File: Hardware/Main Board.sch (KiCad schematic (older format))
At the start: 0 parts

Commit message: Merge Danny's changes to the board, gitignore
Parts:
- added .1uF: C5, symbol CAPACITOR
- added .1uF: C6, symbol CAPACITOR
- added .1uF: C7, symbol CAPACITOR
- added .1uF: C3, symbol CAPACITOR
- added .1uF: C2, symbol CAPACITOR
- added .1uF: C1, symbol CAPACITOR
- added .1uF: C8, symbol CAPACITOR
- added .1uF: C9, symbol CAPACITOR
- added 4.7uF: C4, symbol CAPACITOR
- added C1: 4.7uF, symbol CAPACITOR
- added C2: .1uF, symbol CAPACITOR
- added C3, C4: 15pF, symbol CAPACITOR
- added FB?: FB1, symbol FERRITE
- added U1: STM32F401RCT6, symbol STM32F401RCT6
- added X1: 24MHz, ~, symbol CRYSTAL
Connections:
- net labels added: GND, NRST, OSC_IN, OSC_OUT, Reg+3v3, VDD, VDDA
- wire segments 0 -> 64

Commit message: Add 5v regulator and RS485 transceiver to Main board
Added RS485 and a 5v regulator to power it
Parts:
- added U1: SN75176BDR, symbol SN75176BDR
- .1uF, 4.7uF, C1, C2, C3, C4: symbol CAPACITOR -> Capacitor
- FB?: symbol FERRITE -> Ferrite
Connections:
- net labels added: 485_A, 485_B, GPIO_PC4_Reg1EN, GPIO_PC5_Reg2EN, Reg+3V3, Reg+5V, USART1_RX, USART1_TX
- wire segments 64 -> 83

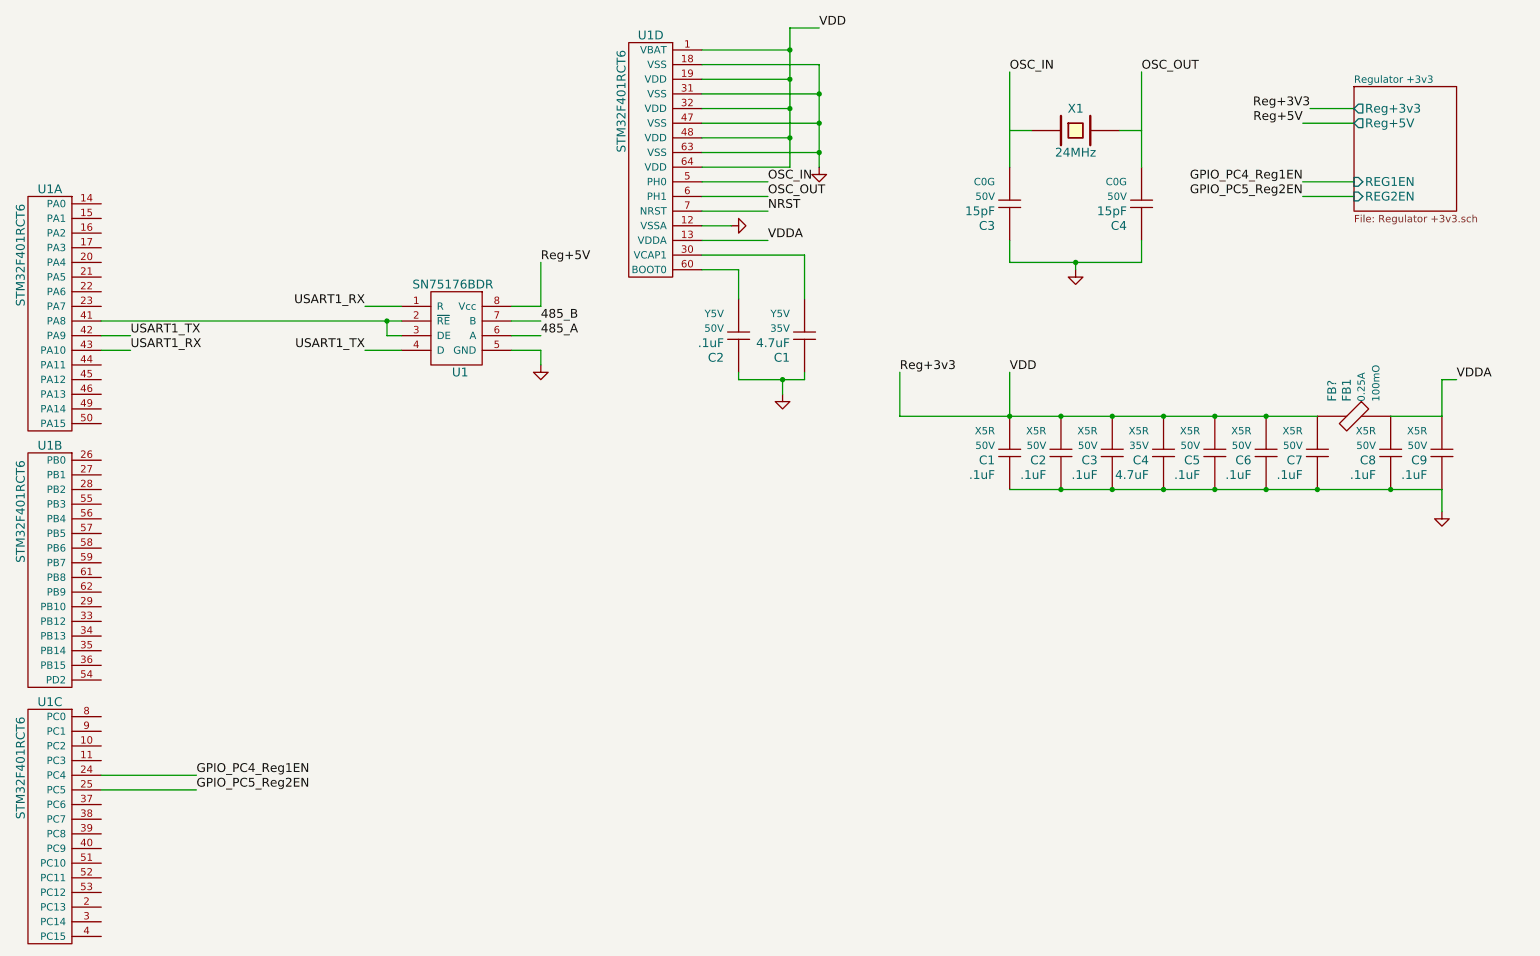
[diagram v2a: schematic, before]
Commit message: Add BTA breakout for Vernier sensors and convert 5v analog to 3v3
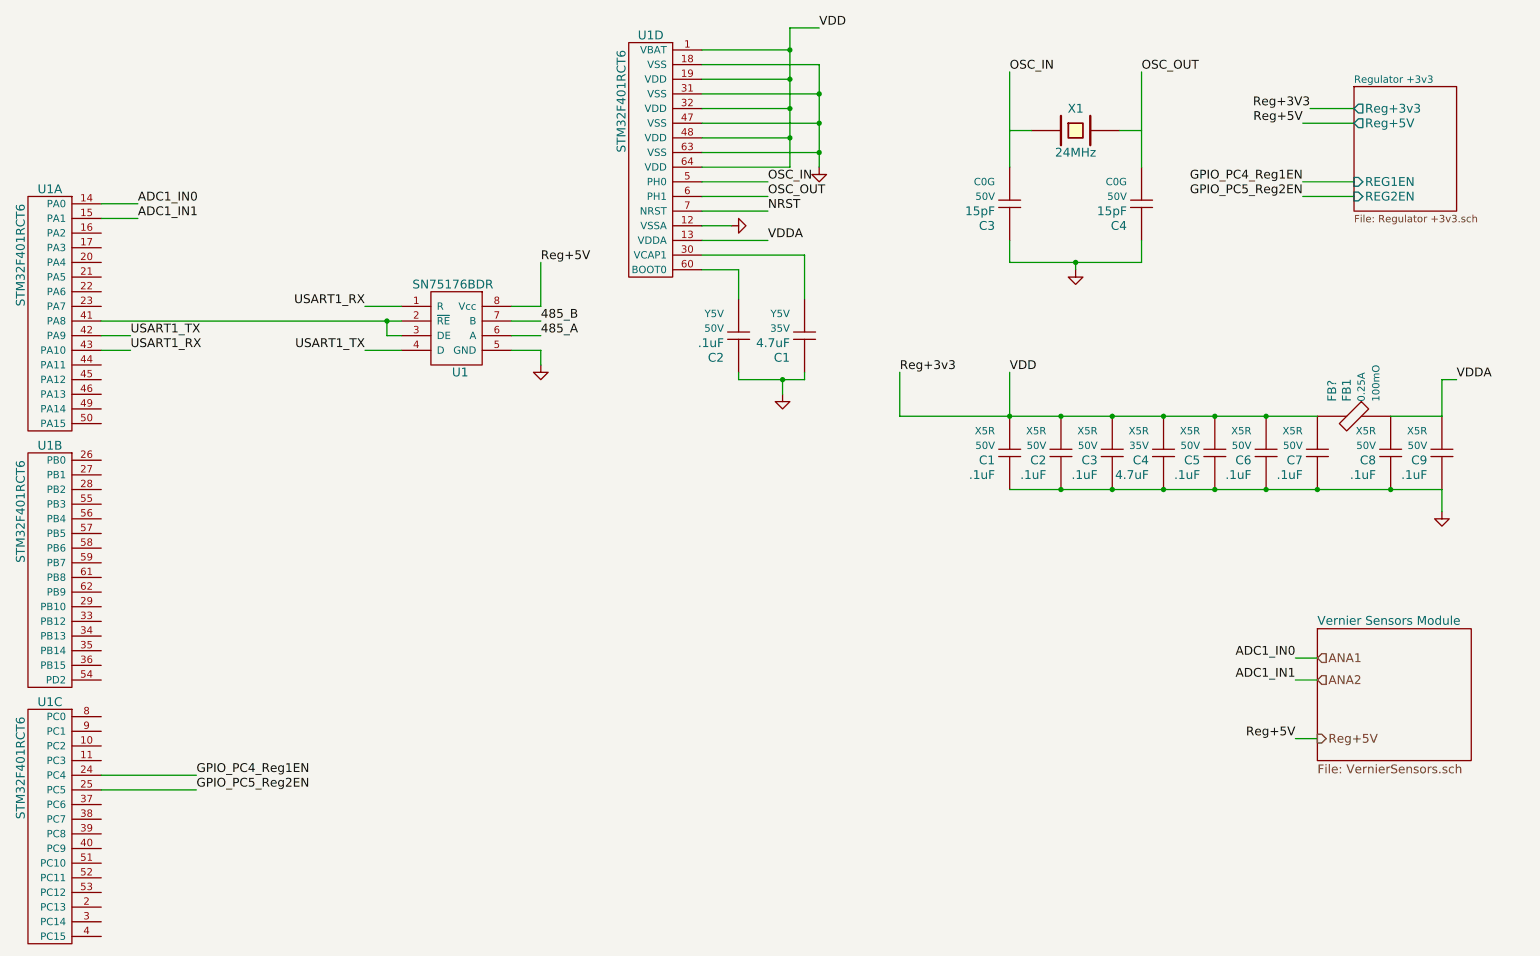
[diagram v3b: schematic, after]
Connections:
- net ANA1: now reaches U1.14 (PA0)
- net ANA2: now reaches U1.15 (PA1)
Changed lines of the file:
@@
 LIBS:device
 LIBS:conn
+LIBS:MAVRIClib
 LIBS:Passives
 LIBS:STMicroelectronics
-LIBS:MAVRIClib
 LIBS:Main Board-cache
 EELAYER 25 0
@@
 $Descr A4 11693 8268
 encoding utf-8
-Sheet 1 2
+Sheet 1 3
 Title ""
 Date "7 mar 2015"
@@
 Text Label 4200 2700 0    60   ~ 0
 485_A
+Text HLabel 9500 5450 2    60   Output ~ 0
+Reg+5V
+Text Label 9350 5450 2    60   ~ 0
+Reg+5V
+$Sheet
+S 9500 4700 1050 900
+U 551DB2D0
+F0 "Vernier Sensors Module" 60
+F1 "VernierSensors.sch" 60
+$EndSheet
+Wire Wire Line
+	9500 5450 9350 5450
+Text HLabel 9500 4900 2    60   Input ~ 0
+ANA1
+Text HLabel 9500 5050 2    60   Input ~ 0
+ANA2
+Wire Wire Line
+	9500 4900 9350 4900
+Wire Wire Line
+	9500 5050 9350 5050
+Text Label 9350 4900 2    60   ~ 0
+ADC1_IN0
+Text Label 9350 5050 2    60   ~ 0
+ADC1_IN1
+Wire Wire Line
+	1200 1800 1450 1800
+Wire Wire Line
+	1450 1900 1200 1900
+Text Label 1450 1900 0    60   ~ 0
+ADC1_IN1
+Text Label 1450 1800 0    60   ~ 0
+ADC1_IN0
 $EndSCHEMATC

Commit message: Add 485 network out, POE for Wheel Pod boards
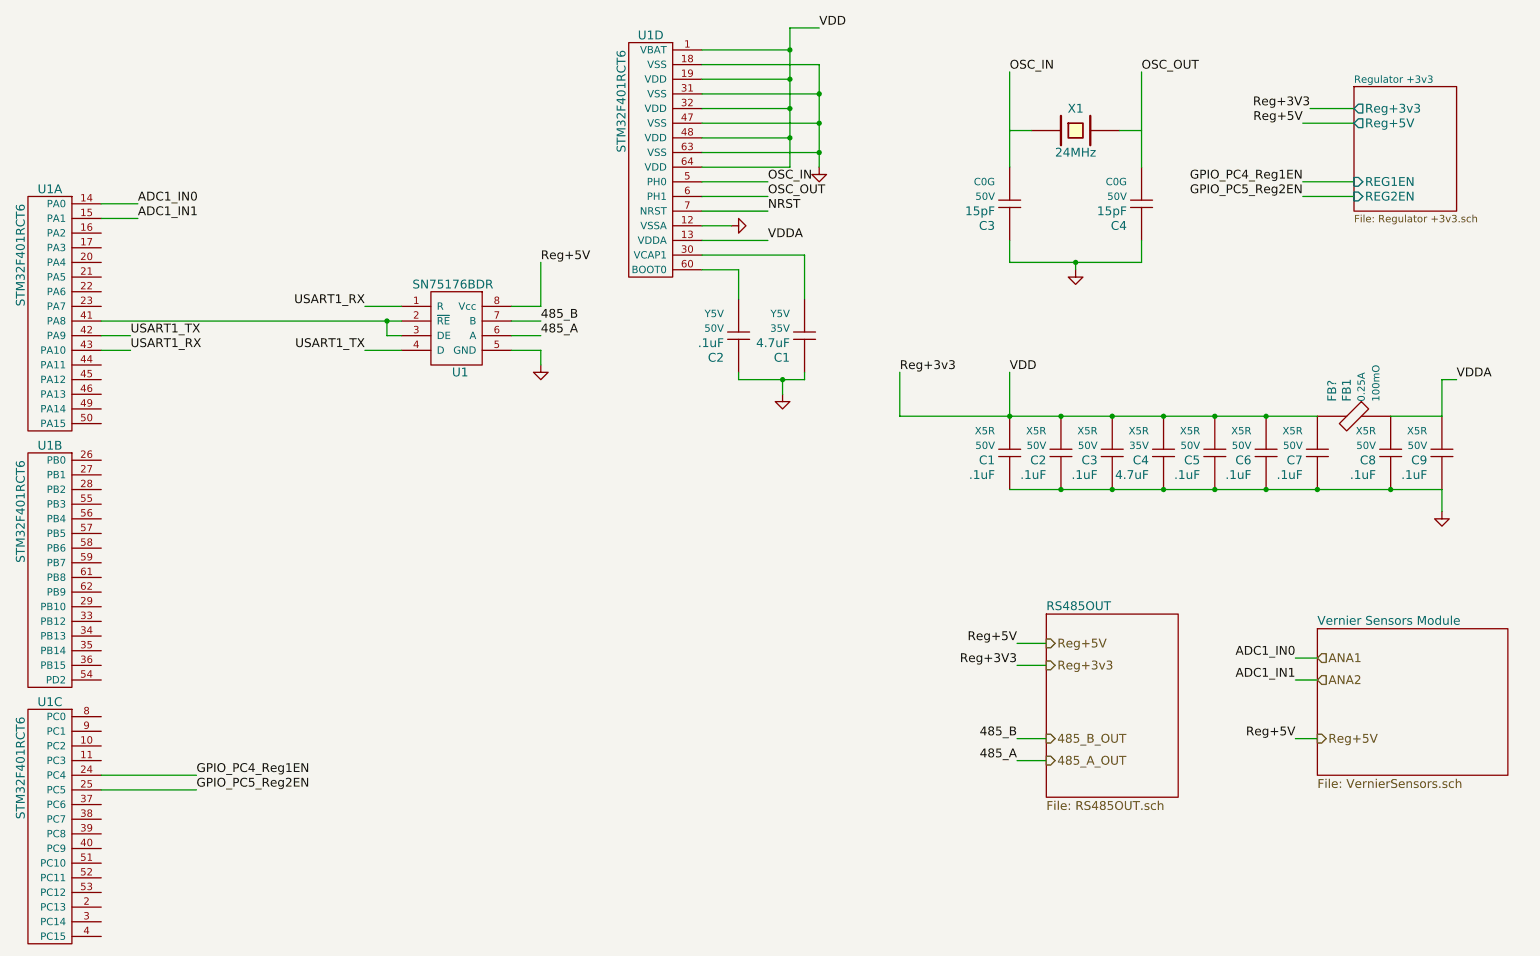
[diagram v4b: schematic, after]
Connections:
- net 485_A renamed 485_A_OUT
- net 485_B renamed 485_B_OUT
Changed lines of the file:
@@
 LIBS:Passives
 LIBS:STMicroelectronics
+LIBS:Connectors
 LIBS:Main Board-cache
 EELAYER 25 0
@@
 $Descr A4 11693 8268
 encoding utf-8
-Sheet 1 3
+Sheet 1 4
 Title ""
 Date "7 mar 2015"
@@
 	1    0    0    -1
 $EndComp
-Wire Wire Line
-	7400 1300 7550 1300
-Wire Wire Line
-	7400 900  7400 1550
-Connection ~ 5850 3000
-Wire Wire Line
-	5550 3000 5850 3000
-Wire Wire Line
-	5850 3000 6000 3000
-Wire Wire Line
-	5550 2950 5550 3000
-Wire Wire Line
-	5850 3000 5850 3100
-Wire Wire Line
-	6000 2150 6000 2450
-Wire Wire Line
-	5550 2250 5550 2450
-Wire Wire Line
-	5300 2250 5550 2250
-Wire Wire Line
-	5300 1650 5750 1650
-Wire Wire Line
-	5300 1750 5750 1750
-Wire Wire Line
-	5300 1850 5750 1850
-Wire Wire Line
-	5300 2050 5750 2050
-Wire Wire Line
-	5300 1950 5500 1950
-Connection ~ 5900 750
-Wire Wire Line
-	5900 600  6100 600
-Connection ~ 6100 1450
-Wire Wire Line
-	6650 3250 7400 3250
-Wire Wire Line
-	7400 3250 7750 3250
-Wire Wire Line
-	7750 3250 8100 3250
-Wire Wire Line
-	8100 3250 8450 3250
-Wire Wire Line
-	8450 3250 8800 3250
-Wire Wire Line
-	8800 3250 9150 3250
-Wire Wire Line
-	9150 3250 9500 3250
-Connection ~ 7750 3250
-Connection ~ 8100 3250
-Connection ~ 8450 3250
-Connection ~ 8800 3250
-Connection ~ 9150 3250
-Wire Wire Line
-	7400 3750 7750 3750
-Wire Wire Line
-	7750 3750 8100 3750
-Wire Wire Line
-	8100 3750 8450 3750
-Wire Wire Line
-	8450 3750 8800 3750
-Wire Wire Line
-	8800 3750 9150 3750
-Wire Wire Line
-	9150 3750 9500 3750
-Wire Wire Line
-	9500 3750 10000 3750
-Wire Wire Line
-	10000 3750 10350 3750
-Connection ~ 7750 3750
-Connection ~ 8100 3750
-Connection ~ 8450 3750
-Connection ~ 8800 3750
-Connection ~ 9150 3750
-Wire Wire Line
-	10000 3250 10350 3250
-Connection ~ 9500 3750
-Connection ~ 10000 3750
-Wire Wire Line
-	7400 2950 7400 3250
-Wire Wire Line
-	6650 3250 6650 2950
-Connection ~ 7400 3250
-Wire Wire Line
-	5300 750  5900 750
-Wire Wire Line
-	5900 950  5300 950
-Wire Wire Line
-	5900 600  5900 750
-Wire Wire Line
-	5900 750  5900 950
-Wire Wire Line
-	5900 950  5900 1150
-Wire Wire Line
-	5900 1150 5900 1350
-Wire Wire Line
-	5900 1350 5900 1550
-Wire Wire Line
-	5900 1150 5300 1150
-Connection ~ 5900 950
-Wire Wire Line
-	5900 1350 5300 1350
-Connection ~ 5900 1150
-Wire Wire Line
-	5900 1550 5300 1550
-Connection ~ 5900 1350
-Wire Wire Line
-	6100 1450 5300 1450
-Wire Wire Line
-	6100 850  6100 1050
-Wire Wire Line
-	6100 1050 6100 1250
-Wire Wire Line
-	6100 1250 6100 1450
-Wire Wire Line
-	6100 1450 6100 1550
-Wire Wire Line
-	6100 1250 5300 1250
-Wire Wire Line
-	6100 1050 5300 1050
-Connection ~ 6100 1250
-Wire Wire Line
-	6100 850  5300 850
-Connection ~ 6100 1050
-Wire Wire Line
-	8300 900  8300 1550
-Wire Wire Line
-	8300 1300 8150 1300
-Wire Wire Line
-	7400 2050 7400 2200
-Wire Wire Line
-	7400 2200 7850 2200
-Wire Wire Line
-	7850 2200 8300 2200
-Wire Wire Line
-	8300 2200 8300 2050
-Wire Wire Line
-	7850 2200 7850 2250
-Connection ~ 7850 2200
-Wire Wire Line
-	9450 1150 9750 1150
-Wire Wire Line
-	5300 2150 6000 2150
-Wire Wire Line
-	6000 3000 6000 2950
-Wire Wire Line
-	10350 3250 10350 3000
-Wire Wire Line
-	10350 3000 10450 3000
-Wire Wire Line
-	10350 3750 10350 3900
-Wire Wire Line
-	4200 2500 4000 2500
-Wire Wire Line
-	4200 2200 4200 2500
-Wire Wire Line
-	9750 1250 9400 1250
-Wire Wire Line
-	1200 5700 1850 5700
-Wire Wire Line
-	1200 5800 1850 5800
-Wire Wire Line
-	9750 1650 9400 1650
-Wire Wire Line
-	9750 1750 9400 1750
-Wire Wire Line
-	3250 2700 3150 2700
-Wire Wire Line
-	3150 2700 3150 2600
-Wire Wire Line
-	1200 2600 3150 2600
-Wire Wire Line
-	3150 2600 3250 2600
-Connection ~ 3150 2600
-Wire Wire Line
-	3250 2800 3000 2800
-Wire Wire Line
-	3250 2500 3000 2500
-Wire Wire Line
-	1200 2700 1400 2700
-Wire Wire Line
-	1200 2800 1400 2800
-Wire Wire Line
-	4000 2800 4200 2800
-Wire Wire Line
-	4200 2800 4200 2900
-Wire Wire Line
-	4000 2600 4200 2600
-Wire Wire Line
-	4000 2700 4200 2700
 Text Label 4200 2600 0    60   ~ 0
 485_B
@@
 Reg+5V
 $Sheet
-S 9500 4700 1050 900
+S 9500 4700 1300 1000
 U 551DB2D0
 F0 "Vernier Sensors Module" 60
 F1 "VernierSensors.sch" 60
 $EndSheet
-Wire Wire Line
-	9500 5450 9350 5450
 Text HLabel 9500 4900 2    60   Input ~ 0
 ANA1
 Text HLabel 9500 5050 2    60   Input ~ 0
 ANA2
-Wire Wire Line
-	9500 4900 9350 4900
-Wire Wire Line
-	9500 5050 9350 5050
 Text Label 9350 4900 2    60   ~ 0
 ADC1_IN0
 Text Label 9350 5050 2    60   ~ 0
 ADC1_IN1
-Wire Wire Line
-	1200 1800 1450 1800
-Wire Wire Line
-	1450 1900 1200 1900
 Text Label 1450 1900 0    60   ~ 0
 ADC1_IN1
 Text Label 1450 1800 0    60   ~ 0
 ADC1_IN0
+Wire Wire Line
+	7400 1300 7550 1300
+Wire Wire Line
+	7400 900  7400 1550
+Connection ~ 5850 3000
+Wire Wire Line
+	5550 3000 6000 3000
+Wire Wire Line
+	5550 2950 5550 3000
+Wire Wire Line
+	5850 3000 5850 3100
+Wire Wire Line
+	6000 2150 6000 2450
+Wire Wire Line
+	5550 2250 5550 2450
+Wire Wire Line
+	5300 2250 5550 2250
+Wire Wire Line
+	5300 1650 5750 1650
+Wire Wire Line
+	5300 1750 5750 1750
+Wire Wire Line
+	5300 1850 5750 1850
+Wire Wire Line
+	5300 2050 5750 2050
+Wire Wire Line
+	5300 1950 5500 1950
+Connection ~ 5900 750
+Wire Wire Line
+	5900 600  6100 600
+Connection ~ 6100 1450
+Wire Wire Line
+	6650 3250 9500 3250
+Connection ~ 7750 3250
+Connection ~ 8100 3250
+Connection ~ 8450 3250
+Connection ~ 8800 3250
+Connection ~ 9150 3250
+Wire Wire Line
+	7400 3750 10350 3750
+Connection ~ 7750 3750
+Connection ~ 8100 3750
+Connection ~ 8450 3750
+Connection ~ 8800 3750
+Connection ~ 9150 3750
+Wire Wire Line
+	10000 3250 10350 3250
+Connection ~ 9500 3750
+Connection ~ 10000 3750
+Wire Wire Line
+	7400 2950 7400 3250
+Wire Wire Line
+	6650 3250 6650 2950
+Connection ~ 7400 3250
+Wire Wire Line
+	5300 750  5900 750
+Wire Wire Line
+	5900 950  5300 950
+Wire Wire Line
+	5900 600  5900 1550
+Wire Wire Line
+	5900 1150 5300 1150
+Connection ~ 5900 950
+Wire Wire Line
+	5900 1350 5300 1350
+Connection ~ 5900 1150
+Wire Wire Line
+	5900 1550 5300 1550
+Connection ~ 5900 1350
+Wire Wire Line
+	6100 1450 5300 1450
+Wire Wire Line
+	6100 850  6100 1550
+Wire Wire Line
+	6100 1250 5300 1250
+Wire Wire Line
+	6100 1050 5300 1050
+Connection ~ 6100 1250
+Wire Wire Line
+	6100 850  5300 850
+Connection ~ 6100 1050
+Wire Wire Line
+	8300 900  8300 1550
+Wire Wire Line
+	8300 1300 8150 1300
+Wire Wire Line
+	7400 2050 7400 2200
+Wire Wire Line
+	7400 2200 8300 2200
+Wire Wire Line
+	8300 2200 8300 2050
+Wire Wire Line
+	7850 2200 7850 2250
+Connection ~ 7850 2200
+Wire Wire Line
+	9450 1150 9750 1150
+Wire Wire Line
+	5300 2150 6000 2150
+Wire Wire Line
+	6000 3000 6000 2950
+Wire Wire Line
+	10350 3250 10350 3000
+Wire Wire Line
+	10350 3000 10450 3000
+Wire Wire Line
+	10350 3750 10350 3900
+Wire Wire Line
+	4200 2500 4000 2500
+Wire Wire Line
+	4200 2200 4200 2500
+Wire Wire Line
+	9750 1250 9400 1250
+Wire Wire Line
+	1200 5700 1850 5700
+Wire Wire Line
+	1200 5800 1850 5800
+Wire Wire Line
+	9750 1650 9400 1650
+Wire Wire Line
+	9750 1750 9400 1750
+Wire Wire Line
+	3250 2700 3150 2700
+Wire Wire Line
+	3150 2700 3150 2600
+Wire Wire Line
+	1200 2600 3250 2600
+Connection ~ 3150 2600
+Wire Wire Line
+	3250 2800 3000 2800
+Wire Wire Line
+	3250 2500 3000 2500
+Wire Wire Line
+	1200 2700 1400 2700
+Wire Wire Line
+	1200 2800 1400 2800
+Wire Wire Line
+	4000 2800 4200 2800
+Wire Wire Line
+	4200 2800 4200 2900
+Wire Wire Line
+	4000 2600 4200 2600
+Wire Wire Line
+	4000 2700 4200 2700
+Wire Wire Line
+	9500 5450 9350 5450
+Wire Wire Line
+	9500 4900 9350 4900
+Wire Wire Line
+	9500 5050 9350 5050
+Wire Wire Line
+	1200 1800 1450 1800
+Wire Wire Line
+	1450 1900 1200 1900
+Text HLabel 7650 5450 2    60   Output ~ 0
+485_B_OUT
+Text HLabel 7650 5600 2    60   Output ~ 0
+485_A_OUT
+Wire Wire Line
+	7650 5450 7450 5450
+Wire Wire Line
+	7650 5600 7450 5600
+Text Label 7450 5450 2    60   ~ 0
+485_B
+Text Label 7450 5600 2    60   ~ 0
+485_A
+Text HLabel 7650 4800 2    60   Output ~ 0
+Reg+5V
+Text HLabel 7650 4950 2    60   Output ~ 0
+Reg+3v3
+Wire Wire Line
+	7650 4800 7450 4800
+Wire Wire Line
+	7650 4950 7450 4950
+Text Label 7450 4950 2    60   ~ 0
+Reg+3V3
+Text Label 7450 4800 2    60   ~ 0
+Reg+5V
+$Sheet
+S 7650 4600 900  1250
+U 55205598
+F0 "RS485OUT" 60
+F1 "RS485OUT.sch" 60
+$EndSheet
 $EndSCHEMATC
